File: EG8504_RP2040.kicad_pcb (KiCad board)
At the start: 2 copper layers, 46 x 90 mm, 53 parts, among them J1 USB_C_Receptacle_USB2.0_16P, J2 522712079, J3 Conn_01x03_Socket, J4 Conn_01x03_Socket, J5 Conn_01x03_Socket, J6 Conn_01x20_Socket, J7 Conn_01x20_Socket, SW1 SW_Push, SW2 SW_Push, U1 RP2040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

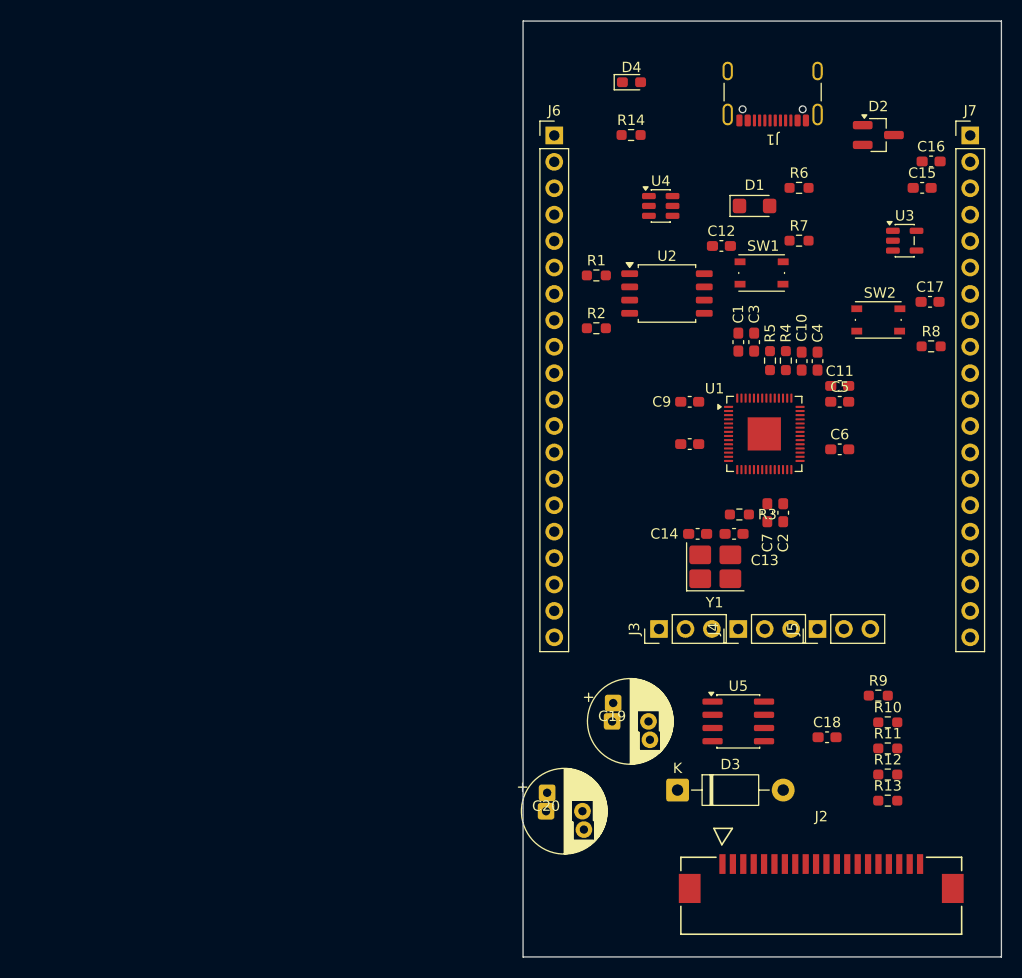
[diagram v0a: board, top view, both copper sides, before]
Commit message: マイコン回りの配線
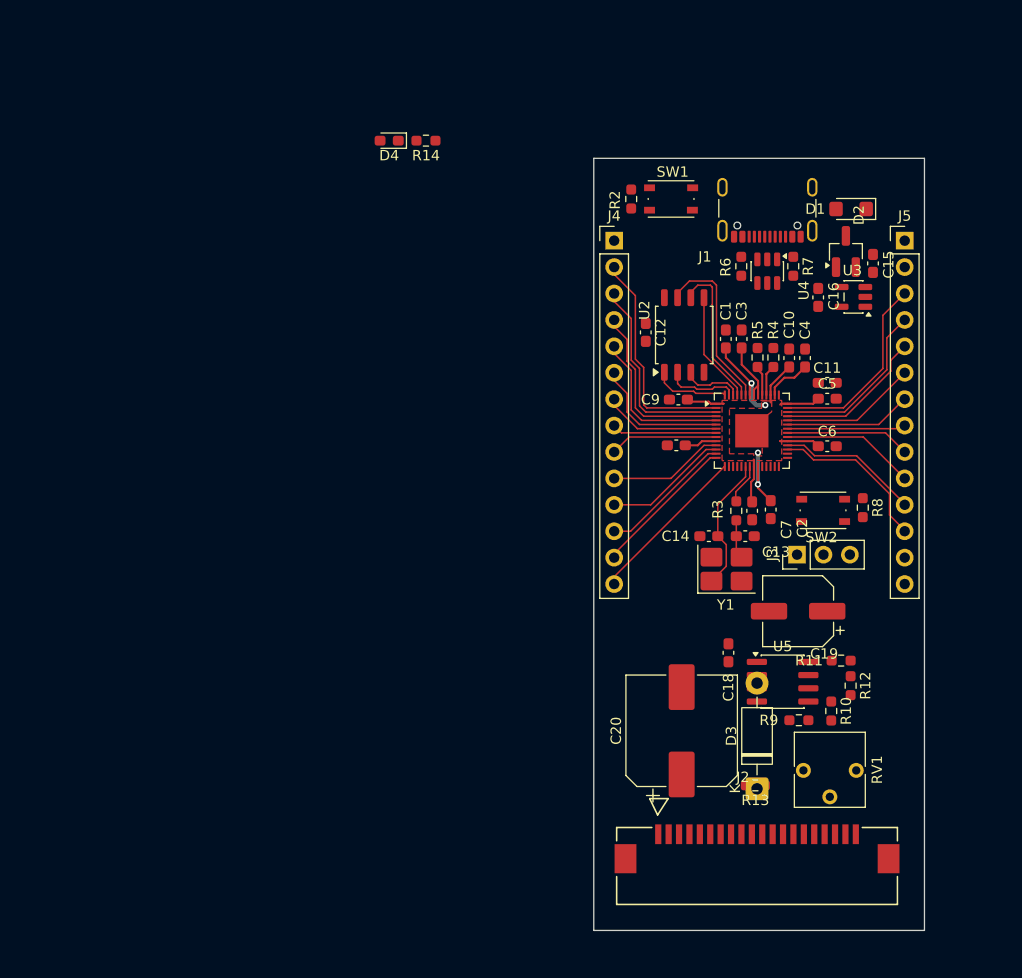
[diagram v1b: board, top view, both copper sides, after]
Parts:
- removed C17: 1u, Capacitor_SMD:C_0603_1608Metric_Pad1.08x0.95mm_HandSolder
- removed J6, J7: Conn_01x20_Socket, Connector_PinHeader_2.54mm:PinHeader_1x20_P2.54mm_Vertical
- removed R1: DNF, Resistor_SMD:R_0603_1608Metric_Pad0.98x0.95mm_HandSolder
- added RV1: 5k, Potentiometer_THT:Potentiometer_Vishay_T73YP_Vertical, F.Cu at (130.0, 122.1)
- C19: footprint MyLibrary:CP_Radial_D8.0mm_P3.50mm_P5.00mm -> Capacitor_SMD:CP_Elec_6.3x5.4
- C20: footprint MyLibrary:CP_Radial_D8.0mm_P3.50mm_P5.00mm -> Capacitor_SMD:CP_Elec_10x10.5
- J4, J5: value Conn_01x03_Socket -> Conn_01x14_Socket; footprint Connector_PinHeader_2.54mm:PinHeader_1x03_P2.54mm_Vertical -> Connector_PinHeader_2.54mm:PinHeader_1x14_P2.54mm_Vertical
- moved J4 39.2 mm to (111.8, 71.1), turned to 0 degrees
- moved J5 38.3 mm to (139.7, 71.1), turned to 0 degrees
- moved D4 24.0 mm to (90.1, 61.5), turned to 180 degrees
- moved C19 20.7 mm to (129.4, 106.8), turned to 180 degrees
- moved R14 19.7 mm to (93.7, 61.5), turned to 180 degrees
- moved SW2 19.1 mm to (131.8, 97.1), turned to 180 degrees
- moved C16 17.0 mm to (131.4, 76.6), turned to 90 degrees
- moved R8 16.8 mm to (135.7, 96.8), turned to -90 degrees
- moved J3 15.1 mm to (129.3, 101.3)
- moved C20 15.1 mm to (118.2, 118.2), turned to 90 degrees
- moved R2 12.9 mm to (113.4, 67.1), turned to -90 degrees
- moved R13 12.8 mm to (125.3, 123.5), turned to 180 degrees
- moved C18 12.5 mm to (122.8, 110.8), turned to 90 degrees
- moved U4 12.0 mm to (126.5, 74.1), turned to -90 degrees
- moved D2 11.6 mm to (134.0, 72.2), turned to 90 degrees
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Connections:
- C20 pad 1: Net-(C20-Pad1) -> /VDOH
- J2 pad 2: /LP -> /GPIO14
- J2 pad 3: /XSCL -> /GPIO15
- J3 pad 1: /GPIO0 -> /SWD
- J3 pad 3: /GPIO1 -> /SWCLK
- J4 pad 1: +5V -> +3.3V
- J4 pad 2: GND -> /GPIO0
- J4 pad 3: +3.3V -> /GPIO1
- J5 pad 1: /SWD -> +5V
- J5 pad 3: /SWCLK -> /GPIO29_ADC3
- R10 pad 2: Net-(C20-Pad1) -> /VDOH
- U1 pad 16: /GPIO13 -> /DIN
- U1 pad 27: /GPIO16 -> /D4
- U1 pad 28: /GPIO17 -> /D5
- U1 pad 29: /GPIO18 -> /D6
- U1 pad 30: /GPIO19 -> /D7
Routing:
- net +3.3V: track 0.00 -> 29.7 mm
- net /GPIO0: track 0.00 -> 21.5 mm
- net +1V1: track 0.00 -> 19.8 mm, vias 0 -> 4
- net /GPIO1: track 0.00 -> 19.4 mm
- net /GPIO29_ADC3: track 0.00 -> 19.0 mm
- net /GPIO2: track 0.00 -> 17.4 mm
- net /GPIO28_ADC2: track 0.00 -> 16.9 mm
- net /QSPI_SD3: track 0.00 -> 16.6 mm
- net /GPIO12: track 0.00 -> 15.7 mm
- net /GPIO20: track 0.00 -> 15.4 mm
- net /GPIO3: track 0.00 -> 15.4 mm
- net /GPIO27_ADC1: track 0.00 -> 15.0 mm
- net /QSPI_SCLK: track 0.00 -> 14.5 mm
- net /GPIO11: track 0.00 -> 14.0 mm
- net /GPIO26_ADC0: track 0.00 -> 13.4 mm
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- added copper zone on F.Cu, net +1V1
- added copper zone on F.Cu, net +3.3V
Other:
- board size 46 x 90 mm -> 31.8 x 74.2 mm

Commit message: sd入れたpsb
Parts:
- removed C1, C12, C2, C3, C4, C5, C6, C7, C8, C9: 100n, Capacitor_SMD:C_0603_1608Metric_Pad1.08x0.95mm_HandSolder
- removed C10, C11: 1u, Capacitor_SMD:C_0603_1608Metric_Pad1.08x0.95mm_HandSolder
- removed C13, C14: 22p, Capacitor_SMD:C_0603_1608Metric_Pad1.08x0.95mm_HandSolder
- removed C15, C16: 10u, Capacitor_SMD:C_0603_1608Metric_Pad1.08x0.95mm_HandSolder
- removed D1: SMF5V0A, Diode_SMD:D_SMF
- removed D2: CH213K, Package_TO_SOT_SMD:SOT-23_Handsoldering
- removed D4: LED_Small, LED_SMD:LED_0603_1608Metric_Pad1.05x0.95mm_HandSolder
- removed J4, J5: Conn_01x14_Socket, Connector_PinHeader_2.54mm:PinHeader_1x14_P2.54mm_Vertical
- removed R14, R3: 1k, Resistor_SMD:R_0603_1608Metric_Pad0.98x0.95mm_HandSolder
- removed R4, R5: 27, Resistor_SMD:R_0603_1608Metric_Pad0.98x0.95mm_HandSolder
- removed R6, R7: 5k1, Resistor_SMD:R_0603_1608Metric_Pad0.98x0.95mm_HandSolder
- removed R8: 10k, Resistor_SMD:R_0603_1608Metric_Pad0.98x0.95mm_HandSolder
- removed SW1: SW_Push, Button_Switch_SMD:SW_Push_1P1T_NO_Vertical_Wuerth_434133025816
- removed U1: RP2040, Package_DFN_QFN:QFN-56-1EP_7x7mm_P0.4mm_EP3.2x3.2mm
- removed U2: W25Q16JVSS, Package_SO:SOIC-8_5.3x5.3mm_P1.27mm
- removed U3: MIC5504-3.3YM5, Package_TO_SOT_SMD:SOT-23-5
- removed U4: USBLC6-2SC6, Package_TO_SOT_SMD:SOT-23-6
- removed Y1: ECS-3225MV-xxx-xx, Crystal:Crystal_SMD_3225-4Pin_3.2x2.5mm_HandSoldering
- added A1: RaspberryPi_Pico, Module:RaspberryPi_Pico_Common_THT, F.Cu at (129.4, 105.7)
- added R1: 10k, Resistor_SMD:R_0603_1608Metric_Pad0.98x0.95mm_HandSolder, F.Cu at (130.3, 96.2)
- J1: value USB_C_Receptacle_USB2.0_16P -> DM1B-DSF-PEJ; footprint Connector_USB:USB_C_Receptacle_GCT_USB4105-xx-A_16P_TopMnt_Horizontal -> MyLibrary:DM1B-DSF-PEJ
- J3: value Conn_01x03_Socket -> Conn_01x02_Socket; footprint Connector_PinHeader_2.54mm:PinHeader_1x03_P2.54mm_Vertical -> Connector_JST:JST_XH_B2B-XH-A_1x02_P2.50mm_Vertical
- R2: value 1k -> 10k
- moved J2 71.9 mm to (60.8, 100.1), turned to -90 degrees
- moved J3 70.9 mm to (60.8, 119.4), turned to -90 degrees
- moved C20 65.8 mm to (66.0, 78.2), turned to 0 degrees
- moved SW2 65.2 mm to (71.8, 122.4), turned to 0 degrees
- moved RV1 64.4 mm to (79.2, 82.5), turned to 90 degrees
- moved R13 58.9 mm to (78.7, 87.5), turned to 0 degrees
- moved D3 56.4 mm to (82.2, 87.7)
- moved C19 55.4 mm to (83.8, 75.4), turned to 0 degrees
- moved R10 51.9 mm to (89.1, 88.1), turned to 180 degrees
- moved R9 50.9 mm to (89.1, 86.3)
- moved R12 49.7 mm to (95.8, 82.8)
- moved R11 49.6 mm to (95.8, 79.4), turned to 90 degrees
- moved U5 48.4 mm to (90.7, 82.6)
- moved C18 45.7 mm to (85.8, 83.8), turned to -90 degrees
- moved R2 35.0 mm to (129.5, 98.2), turned to 180 degrees
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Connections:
- J2 pad 2: /GPIO14 -> /GPIO7
- J2 pad 3: /GPIO15 -> /GPIO8
- J3 pad 1: /SWD -> +5V
- R2 pad 1: Net-(R2-Pad1) -> +3.3V
- R2 pad 2: /QSPI_SS -> /GPIO1
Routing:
- net /DIN: track 0.00 -> 51.6 mm
- net +3.3V: track 29.7 -> 76.9 mm
- net /DAT0: track 0.00 -> 43.4 mm
- net /D4: track 0.00 -> 39.8 mm
- net /CMD: track 0.00 -> 38.7 mm
- net /GPIO7: track 10.4 -> 48.6 mm
- net /CD/DAT3: track 0.00 -> 37.6 mm
- net /CLK: track 0.00 -> 36.6 mm
- net /CD: track 0.00 -> 36.5 mm
- net /GPIO8: track 11.1 -> 46.3 mm
- net /D5: track 0.00 -> 34.8 mm
- net /D6: track 0.00 -> 32.3 mm
- net /D7: track 0.00 -> 29.9 mm
- net /GPIO0: track 21.5 -> 0.00 mm
- net +1V1: track 19.8 -> 0.00 mm, vias 4 -> 0
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- removed copper zone on F.Cu, net +1V1
- removed copper zone on F.Cu, net +3.3V
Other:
- board size 31.8 x 74.2 mm -> 80.5 x 61.6 mm

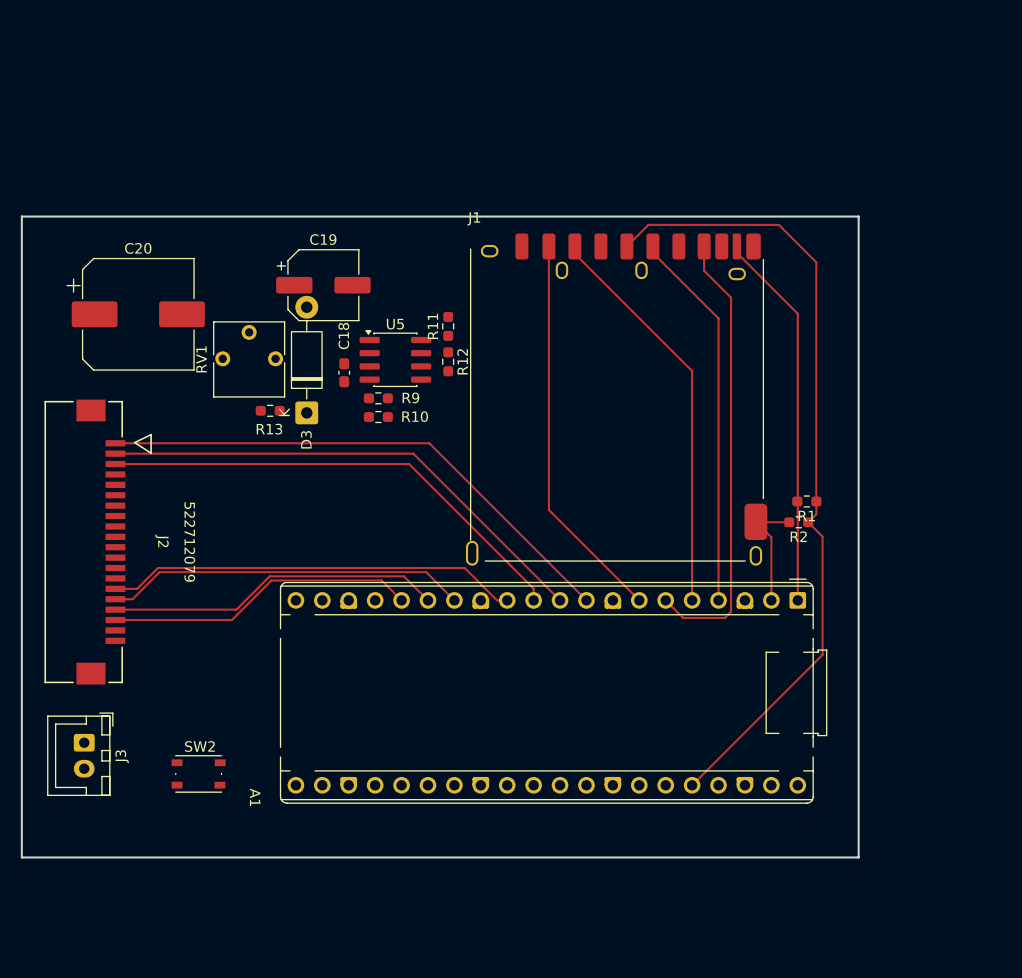
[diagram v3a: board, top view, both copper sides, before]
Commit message: sdの向き違った
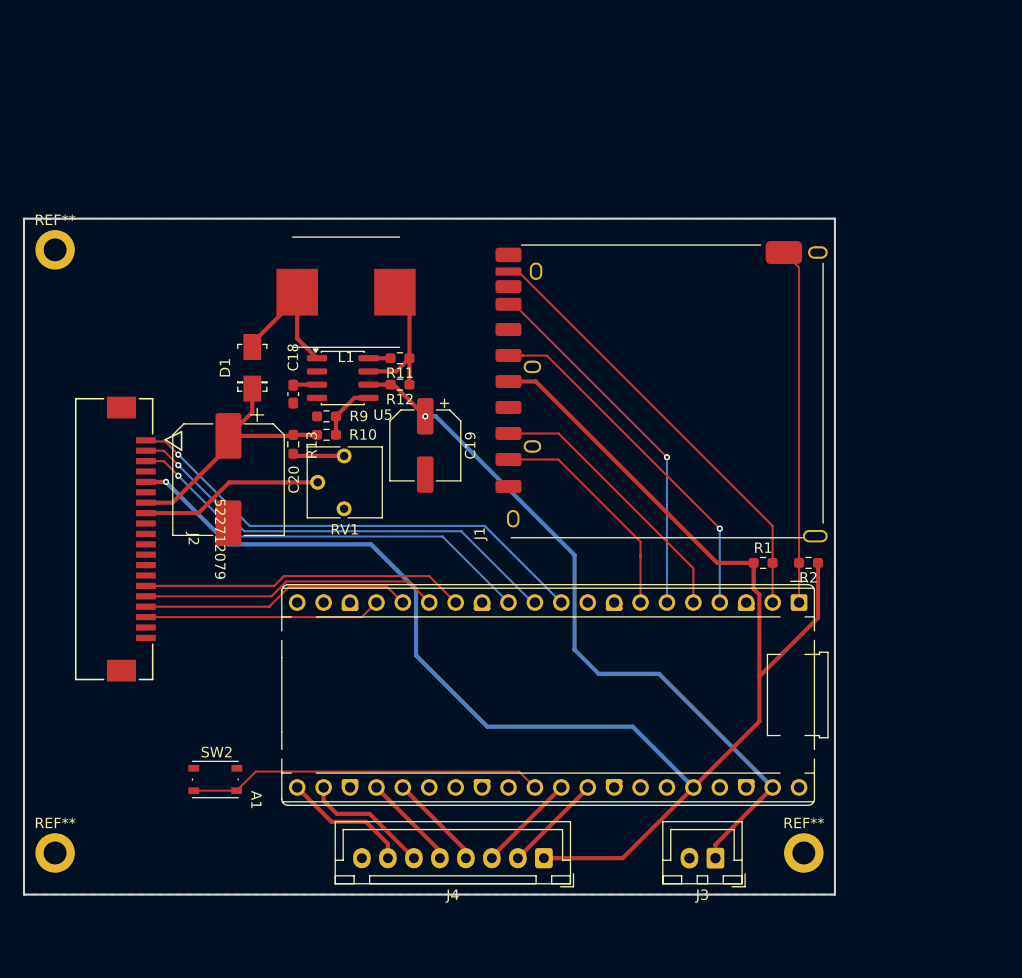
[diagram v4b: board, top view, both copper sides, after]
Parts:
- removed D3: 1N5819, Diode_THT:D_DO-41_SOD81_P10.16mm_Horizontal
- added D1: SS14, digikey-footprints:DO-214AC, F.Cu at (77.0, 83.3)
- added J4: Conn_01x08_Socket, Connector_JST:JST_XH_B8B-XH-A_1x08_P2.50mm_Vertical, F.Cu at (105.0, 130.5)
- added L1: 100u, Inductor_SMD:L_Taiyo-Yuden_NR-10050_9.8x10.0mm_HandSoldering, F.Cu at (86.0, 76.1)
- added REF**: MountingHole_2.2mm_M2_DIN965_Pad, MountingHole:MountingHole_2.2mm_M2_DIN965_Pad, F.Cu at (58.0, 130.0)
- added REF**: MountingHole_2.2mm_M2_DIN965_Pad, MountingHole:MountingHole_2.2mm_M2_DIN965_Pad, F.Cu at (58.0, 72.0)
- added REF**: MountingHole_2.2mm_M2_DIN965_Pad, MountingHole:MountingHole_2.2mm_M2_DIN965_Pad, F.Cu at (130.0, 130.0)
- moved J3 61.7 mm to (121.5, 130.5), turned to 180 degrees
- moved C19 18.3 mm to (93.6, 90.8), turned to -90 degrees
- moved C20 18.1 mm to (74.7, 94.1), turned to -90 degrees
- moved J1 15.6 mm to (102.8, 85.3), turned to 90 degrees
- moved RV1 11.4 mm to (85.8, 91.8), turned to 180 degrees
- moved R1 7.25 mm to (126.1, 102.1), turned to 0 degrees
- moved R11 5.55 mm to (91.2, 82.4), turned to 180 degrees
- moved U5 5.36 mm to (85.7, 84.3)
- moved C18 5.32 mm to (80.9, 85.9)
- moved R9 5.28 mm to (84.1, 88.0)
- moved R10 5.27 mm to (84.1, 89.8)
- moved R12 5.13 mm to (91.2, 85.0), turned to 180 degrees
- moved R2 4.02 mm to (130.5, 102.1)
- moved R13 3.91 mm to (80.9, 90.7), turned to 90 degrees
- moved J2 2.95 mm to (63.7, 99.8)
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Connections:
- A1 pad 1: /CD -> /GPIO0
- A1 pad 10: /GPIO7 -> /DIN
- A1 pad 12: /D4 -> /GPIO9
- A1 pad 14: /D5 -> /D4
- A1 pad 15: /D6 -> /D5
- A1 pad 16: /D7 -> /D6
- A1 pad 17: /GPIO13 -> /D7
- A1 pad 2: /GPIO1 -> /CD
- A1 pad 9: /DIN -> /GPIO6
- J1 pad 11: /GPIO1 -> /GPIO0
- J2 pad 2: /GPIO7 -> /GPIO8
- J2 pad 3: /GPIO8 -> /GPIO9
- R2 pad 2: /GPIO1 -> /GPIO0
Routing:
- net +3.3V: track 76.9 -> 153.7 mm, vias 0 -> 1
- net +5V: track 0.00 -> 69.3 mm, vias 0 -> 1
- net /GPIO7: track 48.6 -> 0.00 mm
- net /GPIO9: track 0.00 -> 40.5 mm, vias 0 -> 1
- net /GPIO0: track 0.00 -> 34.3 mm
- net /RUN: track 0.00 -> 34.2 mm
- net /VDOH: track 0.00 -> 25.3 mm
- net /VLCD: track 0.00 -> 17.7 mm
- net /CD/DAT3: track 37.6 -> 22.2 mm
- net Net-(U5-SwC): track 0.00 -> 14.2 mm
- net Net-(U5-Ipk): track 0.00 -> 13.9 mm
- net /GPIO16: track 0.00 -> 12.3 mm
- net /CMD: track 38.7 -> 26.4 mm
- net /GPIO17: track 0.00 -> 12.2 mm
- net /GPIO1: track 11.4 -> 0.00 mm
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- added copper zone on B.Cu, net GND
- added copper zone on F.Cu, net GND
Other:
- board size 80.5 x 61.6 mm -> 78 x 65 mm
- board text added: "${REFERENCE}"
